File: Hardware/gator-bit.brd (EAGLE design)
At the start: 114.3 x 66 mm, 85 parts, among them J1 GATOR, J19 GATOR, J2 GATOR, J20 GATOR, J21 GATOR, J22 GATOR, J25 GATOR, J28 GATOR, J3 GATOR, J32 GATOR, J33 GATOR, J34 GATOR, J35 GATOR, J36 GATOR, J39 GATOR, J4 GATOR, J40 GATOR, J42 GATOR, U1 5V, U2 micro:bit, U4 MIC5219 3.3V

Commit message: Updated Board File Silk
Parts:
- moved R10 2.54 mm to (22.2, 33.7)
- moved R11 2.54 mm to (22.2, 26.0)
- moved R6 2.54 mm to (22.2, 57.8)
- moved R8 2.54 mm to (22.2, 50.2)
- moved R9 2.54 mm to (22.2, 43.8)
- moved D11 2.54 mm to (26.0, 57.8)
- moved D13 2.54 mm to (26.0, 50.2)
- moved D14 2.54 mm to (26.0, 43.8)
- moved D15 2.54 mm to (26.0, 33.7)
- moved D16 2.54 mm to (26.0, 26.0)
- moved J10 2.54 mm to (21.0, 23.5)
- moved J11 2.54 mm to (21.0, 31.1)
- moved J12 2.54 mm to (21.0, 41.3)
- moved J13 2.54 mm to (21.0, 47.6)
- moved J14 2.54 mm to (21.0, 55.2)
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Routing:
- net P0+: track 31.5 -> 40.4 mm, vias 0 -> 1
- net P14: track 50.5 -> 48.0 mm
- net P20+: track 13.5 -> 16.0 mm
- net P19+: track 13.8 -> 16.3 mm
- net P15+: track 13.8 -> 16.3 mm
- net P14+: track 13.5 -> 16.0 mm
- net P13+: track 13.8 -> 16.3 mm
- net P19: track 62.1 -> 59.6 mm
- net P13: track 50.3 -> 47.7 mm
- net P20: track 65.6 -> 64.5 mm
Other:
- board text added: "3.3V"
- board text added: "5V"
- board text added: "A"
- board text added: "B"
- board text added: "GND"
- board text added: "I2C"
- board text added: "MISO"
- board text added: "MOSI"
- board text added: "Music"
- board text added: "OFF"
- board text added: "ON"
- board text added: "P0"
- board text added: "P1"
- board text added: "P12"
- board text added: "P13"
- board text added: "P14"
- board text added: "P15"
- board text added: "P16"
- board text added: "P19"
- board text added: "P2"
- board text added: "P20"
- board text added: "P8"
- board text added: "POWER IN"
- board text added: "POWER OUT"
- board text added: "SCK"
- board text added: "SCL"
- board text added: "SDA"
- board text added: "SPI"
- board text added: "VIN"

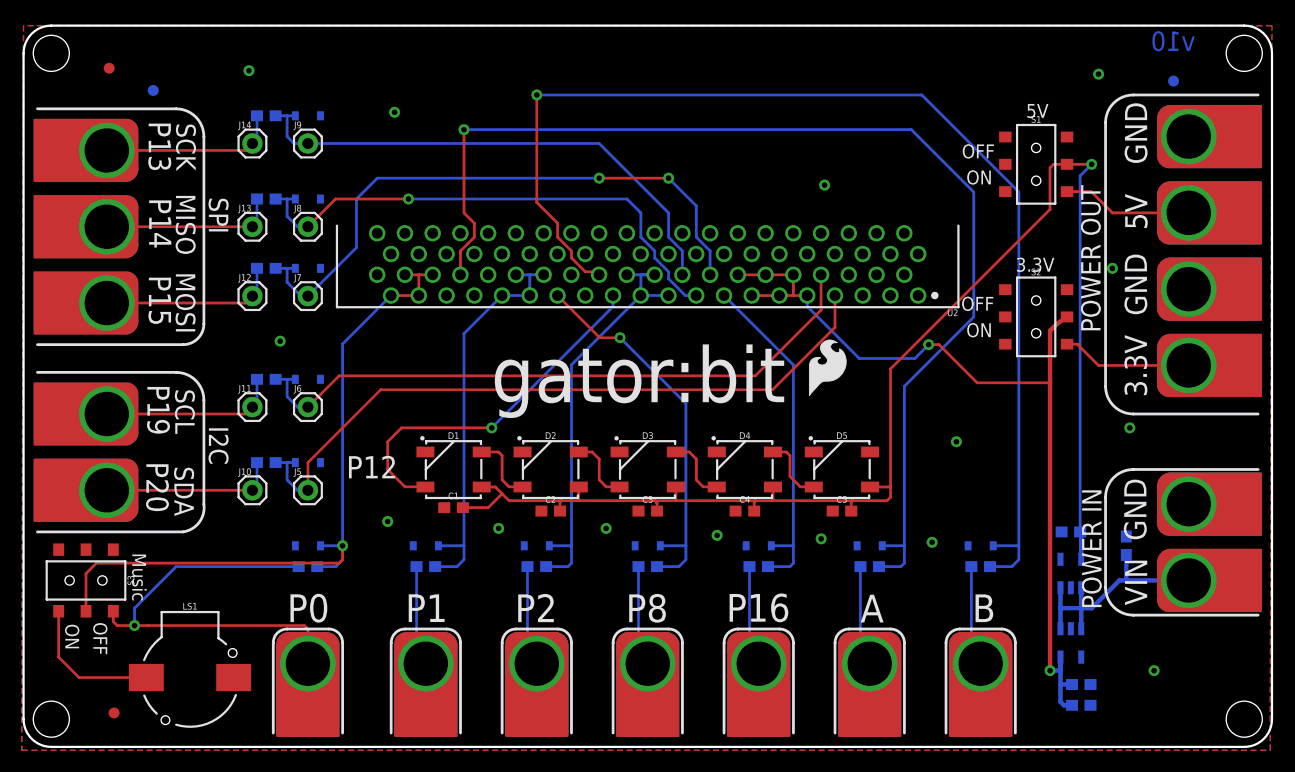
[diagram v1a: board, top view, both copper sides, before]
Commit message: Updating BRD and SCH files -fixed switch problem - isolate speaker and protected pin 0 line -Added silk labels to GPIO -Aesthetics on SCH
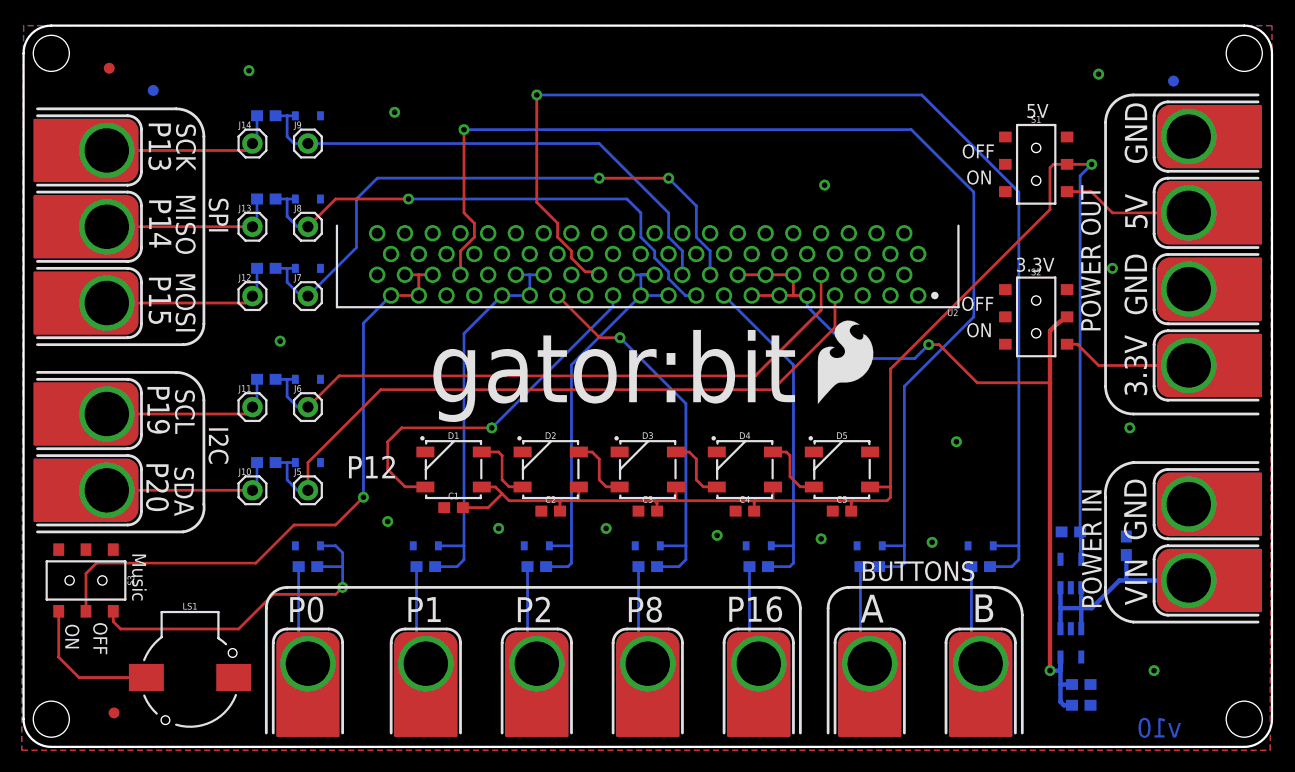
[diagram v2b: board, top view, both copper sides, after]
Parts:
- LOGO1: value SFE_LOGO_FLAME.2_INCH -> SFE_LOGO_FLAME.3_INCH; device SparkFun-Aesthetics:SFE_LOGO_FLAME_.2 -> SparkFun-Aesthetics:SFE_LOGO_FLAME_.3
- moved LOGO1 0.90 mm to (72.2, 31.3)
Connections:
- new net PD: D6.C, R1.2, S3.1
- net P0: no longer D6.C, R1.2
- net P0+: no longer S3.1
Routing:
- net PD: track 0.00 -> 31.6 mm, vias 0 -> 1
- net P0+: track 40.4 -> 9.24 mm, vias 1 -> 0
- net P0: track 66.4 -> 58.3 mm
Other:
- board text added: "BUTTONS"

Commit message: Updated SILK on BRD file
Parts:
- moved FRAME3 56.9 mm to (23.5, -24.8)
- moved FRAME1 15.9 mm to (23.5, -24.8)
- moved U$4 14.9 mm to (1.78, -26.8)
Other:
- board text added: "INPUT/OUTPUT"
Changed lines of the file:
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@@
 <board>
 <plain>
-<text x="55.245" y="-9.525" size="1.778" layer="51" font="vector" ratio="15">Mary West</text>
+<text x="54.61" y="-24.765" size="1.778" layer="51" font="vector" ratio="15">Mary West</text>
 <text x="103.98125" y="1.74625" size="1.778" layer="16" font="vector" ratio="15" rot="SMR0" align="center">v10</text>
 <text x="76.99375" y="89.8525" size="1.778" layer="47" font="vector" ratio="15">* All dimensions
@@
 <dimension x1="111.76" y1="2.54" x2="113.50625" y2="2.54" x3="112.633125" y3="-1.42875" textsize="1.778" layer="47" unit="inch"/>
 <dimension x1="2.54" y1="63.5" x2="0.79375" y2="63.5" x3="1.666875" y3="68.2625" textsize="1.778" layer="47" unit="inch"/>
-<text x="9.398" y="-26.035" size="2.54" layer="51">Solder Mask: Black Gloss</text>
+<text x="4.318" y="-40.64" size="2.54" layer="51">Solder Mask: Black Gloss</text>
 <text x="37.084" y="31.5595" size="6.35" layer="21">gator:bit</text>
 <dimension x1="114.3" y1="67.31" x2="57.15" y2="67.31" x3="85.725" y3="84.455" textsize="1.778" layer="47" unit="inch"/>
@@
 <dimension x1="92.71" y1="53.34" x2="0" y2="53.34" x3="46.355" y3="97.79" textsize="1.778" layer="47" unit="inch"/>
 <dimension x1="92.71" y1="39.37" x2="0" y2="39.37" x3="46.355" y3="101.6" textsize="1.778" layer="47" unit="inch"/>
-<dimension x1="39.37" y1="25.4" x2="0" y2="25.4" x3="19.685" y3="25.4" textsize="1.778" layer="47" unit="inch"/>
-<dimension x1="48.26" y1="25.4" x2="0" y2="25.4" x3="24.13" y3="29.21" textsize="1.778" layer="47" unit="inch"/>
-<dimension x1="57.15" y1="25.4" x2="0" y2="25.4" x3="28.575" y3="33.02" textsize="1.778" layer="47" unit="inch"/>
-<dimension x1="66.04" y1="25.4" x2="0" y2="25.4" x3="33.02" y3="36.83" textsize="1.778" layer="47" unit="inch"/>
-<dimension x1="74.93" y1="25.4" x2="0" y2="25.4" x3="37.465" y3="43.18" textsize="1.778" layer="47" unit="inch"/>
+<dimension x1="39.37" y1="25.4" x2="0" y2="25.4" x3="19.685" y3="83.82" textsize="1.778" layer="47" unit="inch"/>
+<dimension x1="48.26" y1="25.4" x2="0" y2="25.4" x3="24.13" y3="73.025" textsize="1.778" layer="47" unit="inch"/>
+<dimension x1="57.15" y1="25.4" x2="0" y2="25.4" x3="28.575" y3="85.09" textsize="1.778" layer="47" unit="inch"/>
+<dimension x1="66.04" y1="25.4" x2="0" y2="25.4" x3="33.02" y3="68.58" textsize="1.778" layer="47" unit="inch"/>
+<dimension x1="74.93" y1="25.4" x2="0" y2="25.4" x3="37.465" y3="76.2" textsize="1.778" layer="47" unit="inch"/>
 <dimension x1="57.1412375" y1="48.947525" x2="0" y2="49.061828125" x3="28.652865625" y3="90.12030625" textsize="1.778" layer="47" unit="inch"/>
 <text x="91.77929375" y="57.5961" size="1.27" layer="21" font="vector" ratio="15">5V</text>
@@
 <wire x1="103.505" y1="13.335" x2="104.775" y2="12.065" width="0.254" layer="21" curve="90"/>
 <wire x1="104.775" y1="12.065" x2="113.03" y2="12.065" width="0.254" layer="21"/>
+<wire x1="38.1" y1="20.32" x2="34.925" y2="23.495" width="0.254" layer="21" curve="-90"/>
+<wire x1="34.925" y1="23.495" x2="34.925" y2="26.035" width="0.254" layer="21"/>
+<wire x1="34.925" y1="26.035" x2="38.735" y2="29.845" width="0.254" layer="21" curve="-90"/>
+<wire x1="38.735" y1="29.845" x2="77.47" y2="29.845" width="0.254" layer="21"/>
+<wire x1="77.47" y1="29.845" x2="80.01" y2="27.305" width="0.254" layer="21" curve="-90"/>
+<wire x1="80.01" y1="27.305" x2="80.01" y2="22.225" width="0.254" layer="21"/>
+<wire x1="80.01" y1="22.225" x2="78.105" y2="20.32" width="0.254" layer="21" curve="-90"/>
+<wire x1="78.105" y1="20.32" x2="38.1" y2="20.32" width="0.254" layer="21"/>
+<text x="38.51544375" y="15.204596875" size="1.778" layer="21" font="vector" ratio="15">INPUT/OUTPUT</text>
 </plain>
 <attributes>
@@
 </autorouter>
 <elements>
-<element name="FRAME1" library="SparkFun-Aesthetics" package="CREATIVE_COMMONS" value="FRAME-LETTER" x="23.495" y="-8.89"/>
+<element name="FRAME1" library="SparkFun-Aesthetics" package="CREATIVE_COMMONS" value="FRAME-LETTER" x="23.495" y="-24.765"/>
 <element name="FD1" library="SparkFun-Aesthetics" package="FIDUCIAL-1X2" value="FIDUCIAL1X2" x="8.28675" y="3.1115"/>
 <element name="FD2" library="SparkFun-Aesthetics" package="FIDUCIAL-1X2" value="FIDUCIAL1X2" x="7.84225" y="62.13475" smashed="yes"/>
@@
 <attribute name="PROD_ID" value="CONN-13452" x="57.1412375" y="48.947525" size="1.778" layer="27" rot="R180" display="off"/>
 </element>
-<element name="U$4" library="SparkFun-Aesthetics" package="ORDERING_INSTRUCTIONS" value="" x="4.953" y="-12.192"/>
+<element name="U$4" library="SparkFun-Aesthetics" package="ORDERING_INSTRUCTIONS" value="" x="1.778" y="-26.797"/>
 <element name="J19" library="TAB" package="GATOR" value="GATOR" x="106.68" y="34.925" rot="R90"/>
 <element name="J20" library="TAB" package="GATOR" value="GATOR" x="26.035" y="7.62"/>
@@
 <attribute name="PROD_ID" value="VREG-09872" x="92.075" y="2.54" size="1.778" layer="28" rot="MR180" display="off"/>
 </element>
-<element name="FRAME3" library="SparkFun-Aesthetics" package="CREATIVE_COMMONS" value="FRAME-LETTER" x="16.51" y="-81.28"/>
+<element name="FRAME3" library="SparkFun-Aesthetics" package="CREATIVE_COMMONS" value="FRAME-LETTER" x="23.495" y="-24.765"/>
 <element name="U1" library="SparkFun-IC-Power" package="SOT23-5" value="5V" x="95.885" y="15.875" rot="MR0">
 <attribute name="PROD_ID" value="VREG-00823" x="95.885" y="15.875" size="1.778" layer="28" rot="MR0" display="off"/>
